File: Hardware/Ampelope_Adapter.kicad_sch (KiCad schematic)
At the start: 6 parts, among them J1 Conn_01x12_Male, J2 Conn_01x12_Male, J3 Conn_01x12_Male, J4 Conn_01x12_Male, J5 Midi_Board_Connector, J6 Filter_Connector

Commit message: Fixes to Adapter Board
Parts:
- added D1: 3d_Model_Components, Custom_Footprints:3D_Dummy, symbol Mountjoy:3d_Model_Dummy
- added D2: 3d_Model_Controls, Custom_Footprints:3D_Dummy, symbol Mountjoy:3d_Model_Dummy
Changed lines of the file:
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@@
     (pin "1")
+  )
+  (symbol (lib_id "Mountjoy:3d_Model_Dummy") (at 93.98 80.01 0) (unit 1)
+    (in_bom yes) (on_board yes)
+    (property "Reference" "D2" (id 0) (at 95.25 78.7399 0)
+      (effects (font (size 1.27 1.27)) (justify left))
+    )
+    (property "Value" "3d_Model_Controls" (id 1) (at 99.06 78.74 0)
+      (effects (font (size 1.27 1.27)) (justify left))
+    )
+    (property "Footprint" "Custom_Footprints:3D_Dummy" (id 2) (at 93.98 80.01 0)
+      (effects (font (size 1.27 1.27)) hide)
+    )
+    (property "Datasheet" "" (id 3) (at 93.98 80.01 0)
+      (effects (font (size 1.27 1.27)) hide)
+    )
   )
   (symbol (lib_id "power:+3.3V") (at 26.924 29.718 270) (unit 1)
@@
     )
     (pin "1")
+  )
+  (symbol (lib_id "Mountjoy:3d_Model_Dummy") (at 93.98 77.47 0) (unit 1)
+    (in_bom yes) (on_board yes)
+    (property "Reference" "D1" (id 0) (at 95.25 76.1999 0)
+      (effects (font (size 1.27 1.27)) (justify left))
+    )
+    (property "Value" "3d_Model_Components" (id 1) (at 99.06 76.2 0)
+      (effects (font (size 1.27 1.27)) (justify left))
+    )
+    (property "Footprint" "Custom_Footprints:3D_Dummy" (id 2) (at 93.98 77.47 0)
+      (effects (font (size 1.27 1.27)) hide)
+    )
+    (property "Datasheet" "" (id 3) (at 93.98 77.47 0)
+      (effects (font (size 1.27 1.27)) hide)
+    )
   )
   (symbol (lib_id "power:GND") (at 35.814 37.338 90) (unit 1)
@@
       (reference "#PWR015") (unit 1) (value "GND") (footprint "")
     )
+    (path "/7ca7fcf6-b93e-47dc-802f-3e33d368cb67"
+      (reference "D1") (unit 1) (value "3d_Model_Components") (footprint "Custom_Footprints:3D_Dummy")
+    )
+    (path "/1c427bb1-a149-43d6-87fa-3e639b8ffc03"
+      (reference "D2") (unit 1) (value "3d_Model_Controls") (footprint "Custom_Footprints:3D_Dummy")
+    )
     (path "/9139148f-f294-4498-9cbe-e036b9225dd9"

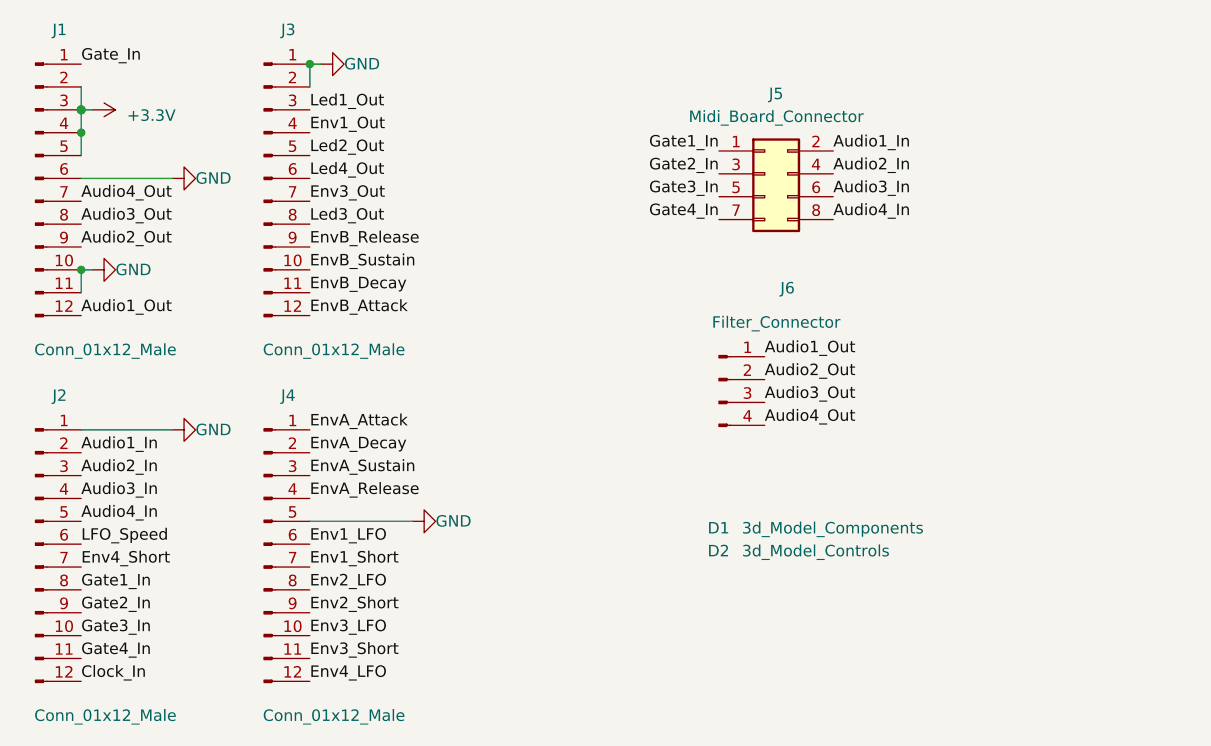
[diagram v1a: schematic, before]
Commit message: Added dummy connector
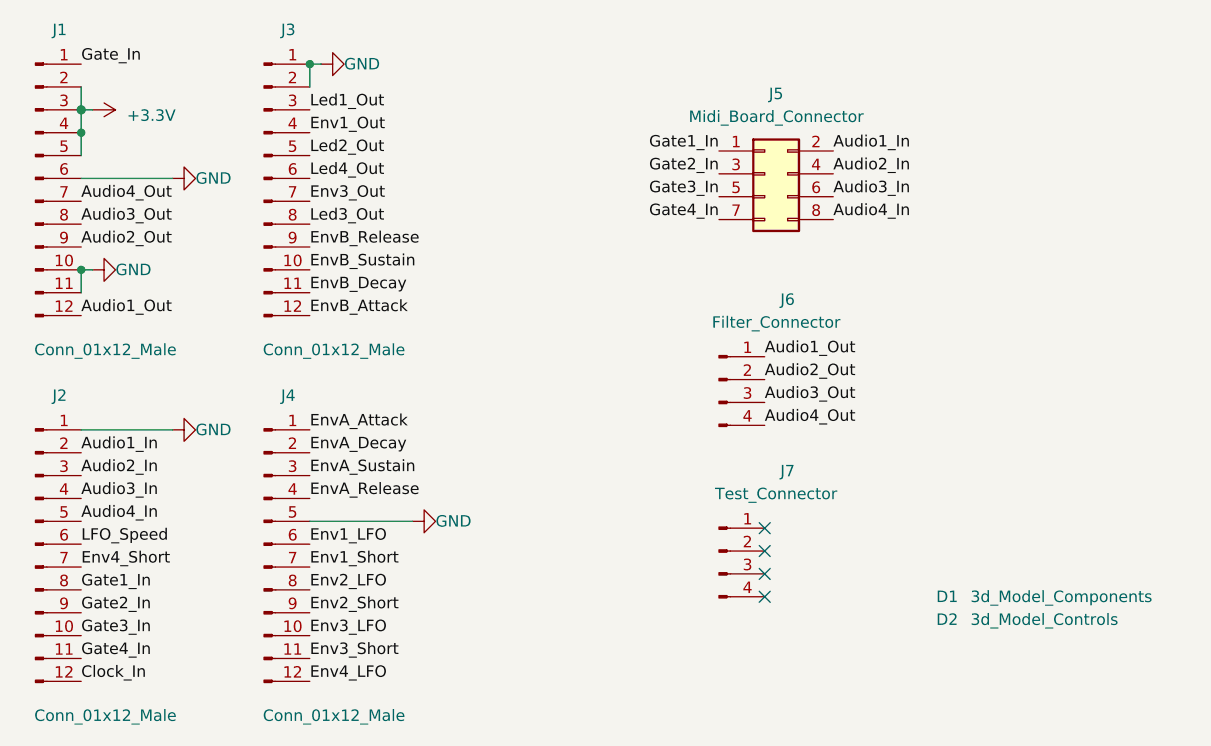
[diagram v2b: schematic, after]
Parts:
- added J7: Test_Connector, Connector_PinHeader_2.54mm:PinHeader_1x04_P2.54mm_Vertical, symbol Connector:Conn_01x04_Male
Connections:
- no-connect marks 0 -> 4
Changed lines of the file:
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@@
   (junction (at 25.654 29.718) (diameter 1.016) (color 0 0 0 0)
   )
+  (no_connect (at 101.6 81.28))
+  (no_connect (at 101.6 83.82))
+  (no_connect (at 101.6 76.2))
+  (no_connect (at 101.6 78.74))
   (wire (pts (xy 25.654 47.498) (xy 26.924 47.498))
     (stroke (width 0) (type solid) (color 0 0 0 0))
@@
   (symbol (lib_id "Mountjoy:3d_Model_Dummy") (at 93.98 80.01 0) (unit 1)
     (in_bom yes) (on_board yes)
-    (property "Reference" "D2" (id 0) (at 95.25 78.7399 0)
+    (property "Reference" "D2" (id 0) (at 120.65 86.3599 0)
       (effects (font (size 1.27 1.27)) (justify left))
     )
-    (property "Value" "3d_Model_Controls" (id 1) (at 99.06 78.74 0)
+    (property "Value" "3d_Model_Controls" (id 1) (at 124.46 86.36 0)
       (effects (font (size 1.27 1.27)) (justify left))
     )
@@
     (pin "1")
   )
-  (symbol (lib_id "Mountjoy:3d_Model_Dummy") (at 93.98 77.47 0) (unit 1)
-    (in_bom yes) (on_board yes)
-    (property "Reference" "D1" (id 0) (at 95.25 76.1999 0)
+  (symbol (lib_id "Connector:Conn_01x04_Male") (at 96.52 78.74 0) (unit 1)
+    (in_bom yes) (on_board yes)
+    (property "Reference" "J7" (id 0) (at 104.14 69.85 0))
+    (property "Value" "Test_Connector" (id 1) (at 102.87 72.39 0))
+    (property "Footprint" "Connector_PinHeader_2.54mm:PinHeader_1x04_P2.54mm_Vertical" (id 2) (at 96.52 78.74 0)
+      (effects (font (size 1.27 1.27)) hide)
+    )
+    (property "Datasheet" "~" (id 3) (at 96.52 78.74 0)
+      (effects (font (size 1.27 1.27)) hide)
+    )
+    (pin "1")
+    (pin "2")
+    (pin "3")
+    (pin "4")
+  )
+  (symbol (lib_id "Mountjoy:3d_Model_Dummy") (at 119.38 85.09 0) (unit 1)
+    (in_bom yes) (on_board yes)
+    (property "Reference" "D1" (id 0) (at 120.65 83.8199 0)
       (effects (font (size 1.27 1.27)) (justify left))
     )
-    (property "Value" "3d_Model_Components" (id 1) (at 99.06 76.2 0)
+    (property "Value" "3d_Model_Components" (id 1) (at 124.46 83.82 0)
       (effects (font (size 1.27 1.27)) (justify left))
     )
-    (property "Footprint" "Custom_Footprints:3D_Dummy" (id 2) (at 93.98 77.47 0)
-      (effects (font (size 1.27 1.27)) hide)
-    )
-    (property "Datasheet" "" (id 3) (at 93.98 77.47 0)
+    (property "Footprint" "Custom_Footprints:3D_Dummy" (id 2) (at 119.38 85.09 0)
+      (effects (font (size 1.27 1.27)) hide)
+    )
+    (property "Datasheet" "" (id 3) (at 119.38 85.09 0)
       (effects (font (size 1.27 1.27)) hide)
     )
@@
   (symbol (lib_id "Connector:Conn_01x04_Male") (at 96.52 59.69 0) (unit 1)
     (in_bom yes) (on_board yes)
-    (property "Reference" "J6" (id 0) (at 104.14 49.53 0))
+    (property "Reference" "J6" (id 0) (at 104.14 50.8 0))
     (property "Value" "Filter_Connector" (id 1) (at 102.87 53.34 0))
     (property "Footprint" "Connector_PinHeader_2.54mm:PinHeader_1x04_P2.54mm_Vertical" (id 2) (at 96.52 59.69 0)
@@
       (reference "J6") (unit 1) (value "Filter_Connector") (footprint "Connector_PinHeader_2.54mm:PinHeader_1x04_P2.54mm_Vertical")
     )
-  )
+    (path "/644000e4-8f43-4f21-adc5-dbf6d8c440a6"
+      (reference "J7") (unit 1) (value "Test_Connector") (footprint "Connector_PinHeader_2.54mm:PinHeader_1x04_P2.54mm_Vertical")
+    )
+  )
